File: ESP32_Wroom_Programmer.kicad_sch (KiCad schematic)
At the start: 19 parts, among them J1 USB_C_Receptacle_USB2.0_16P, Q1 SS8050, Q2 SS8050, U1 CH340C, U3 Torex Semicon XC6206P332MR-G

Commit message: first version of PCB finished!
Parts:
- removed U3: Torex Semicon XC6206P332MR-G, Custom:SOT_23, symbol Custom:Torex_Semicon_XC6206P332MR-G
- added U1: Torex Semicon XC6206P332MR-G, Package_TO_SOT_SMD:SOT-23, symbol Custom:Torex_Semicon_XC6206P332MR-G
- C1: renamed from C2; footprint (none) -> Capacitor_SMD:C_0805_2012Metric
- C2: renamed from C3; footprint (none) -> Capacitor_SMD:C_0805_2012Metric
- C3: renamed from C1; footprint (none) -> Capacitor_SMD:C_0805_2012Metric
- D1: renamed from PWR; footprint (none) -> LED_SMD:LED_0805_2012Metric
- D2: renamed from ACT; footprint (none) -> LED_SMD:LED_0805_2012Metric
- J1: footprint (none) -> Connector_USB:USB_C_Receptacle_GCT_USB4105-xx-A_16P_TopMnt_Horizontal
- J2: renamed from PROG; footprint Connector_JST:JST_EH_B6B-EH-A_1x06_P2.50mm_Vertical -> Connector_PinHeader_2.54mm:PinHeader_1x06_P2.54mm_Horizontal
- R1: renamed from R4; footprint (none) -> Resistor_SMD:R_0805_2012Metric
- R2: renamed from R7; footprint (none) -> Resistor_SMD:R_0805_2012Metric
- R3, R5, R8: footprint (none) -> Resistor_SMD:R_0805_2012Metric
- R4: renamed from R1; footprint (none) -> Resistor_SMD:R_0603_1608Metric
- R6: renamed from R2; footprint (none) -> Resistor_SMD:R_0603_1608Metric
- R7: renamed from R6; footprint (none) -> Resistor_SMD:R_0805_2012Metric
- renumbered U1 to U2
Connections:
- net +3V3: now also U1.2 (Vout)
- net Conv_Tx: now also R8.1
- net GND: now also U1.3 (GND)
- net Prog_Rx: now also J2.4 (Pin_4); no longer J2.5 (Pin_5)
- net Prog_Tx: now also J2.5 (Pin_5); no longer J2.4 (Pin_4), R8.1
- net VBUS: now also U1.1 (Vin)

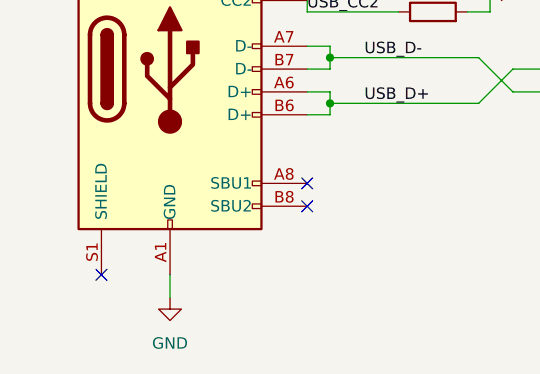
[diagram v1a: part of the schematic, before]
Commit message: added ground to USB-C Shield
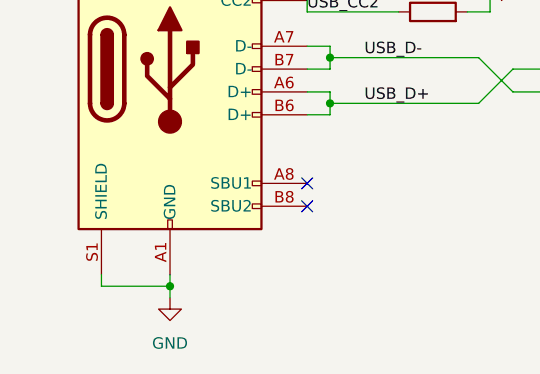
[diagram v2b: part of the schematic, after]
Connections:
- net GND: now also J1.S1 (SHIELD)
- no-connect marks 8 -> 7
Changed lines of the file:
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@@
+	)
+	(junction
+		(at 35.56 158.75)
+		(diameter 0)
+		(color 0 0 0 0)
 	)
 	(junction
@@
 	)
 	(no_connect
-		(at 27.94 157.48)
-	)
-	(no_connect
 		(at 50.8 149.86)
 	)
@@
 	(wire
 		(pts
+			(xy 27.94 157.48) (xy 27.94 158.75)
+		)
+		(stroke
+			(width 0)
+			(type default)
+		)
+	)
+	(wire
+		(pts
 			(xy 198.12 50.8) (xy 208.28 50.8)
 		)
@@
 	(wire
 		(pts
+			(xy 35.56 158.75) (xy 35.56 157.48)
+		)
+		(stroke
+			(width 0)
+			(type default)
+		)
+	)
+	(wire
+		(pts
 			(xy 222.25 128.27) (xy 222.25 125.73)
 		)
@@
 	(wire
 		(pts
-			(xy 35.56 160.02) (xy 35.56 157.48)
+			(xy 35.56 160.02) (xy 35.56 158.75)
 		)
 		(stroke
@@
 		)
 		(stroke
+			(width 0)
+			(type default)
+		)
+	)
+	(wire
+		(pts
+			(xy 27.94 158.75) (xy 35.56 158.75)
+		)
+		(stroke
